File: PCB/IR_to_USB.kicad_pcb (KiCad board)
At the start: 2 copper layers, 120.7 x 44.4 mm, 5 parts, among them U1 STM32F070CBT6

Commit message: PCB in progress
Signed-off-by: denis-m-tyurin <denis.m.turin@gmail.com>
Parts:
- added C5: 100 nF, Capacitors_SMD:C_1206_HandSoldering, F.Cu at (145.2, 94.4)
- added C6: 100 nF, Capacitors_SMD:C_1206_HandSoldering, F.Cu at (136.6, 76.3)
- added C7: 100 nF, Capacitors_SMD:C_1206_HandSoldering, F.Cu at (130.6, 88.5)
- added C8: 100 nF, Capacitors_SMD:C_1206_HandSoldering, F.Cu at (130.4, 79.2)
- added D1: LED_RGB, LEDs:LED_RGB_PLLC-6, F.Cu at (122.1, 95.3)
- added JP1: JUMPER, Buttons_Switches_ThroughHole:SW_DIP_x1_Slide, F.Cu at (138.7, 72.7)
- added P1: CONN_01X06, Connect:PINHEAD1-6, F.Cu at (153.0, 70.9)
- added P2: USB_OTG, Connect:USB_Mini-B, F.Cu at (171.1, 100.8)
- added R1: 10K, Resistors_SMD:R_1206_HandSoldering, F.Cu at (142.4, 74.2)
- added R2: 10K, Resistors_SMD:R_1206_HandSoldering, F.Cu at (128.4, 74.2)
- added R3: 62, Resistors_SMD:R_1206_HandSoldering, F.Cu at (130.1, 94.3)
- added R4: 5, Resistors_SMD:R_1206_HandSoldering, F.Cu at (130.1, 97.3)
- added R5: 5, Resistors_SMD:R_1206_HandSoldering, F.Cu at (130.2, 100.6)
- added R6: 33, Resistors_SMD:R_1206_HandSoldering, F.Cu at (156.9, 94.5)
- added R7: 33, Resistors_SMD:R_1206_HandSoldering, F.Cu at (163.6, 90.2)
- added SW1: SW_PUSH, Buttons_Switches_ThroughHole:SW_PUSH-12mm, F.Cu at (121.2, 84.7)
- added U2: STM32F070CBT6, Housings_QFP:LQFP-48_7x7mm_Pitch0.5mm, F.Cu at (140.9, 85.8)
- added U3: TSOP48, TO_SOT_Packages_THT:TO-220_Neutral123_Horizontal_LargePads, F.Cu at (140.2, 100.3)
- added X1: CRYSTAL_SMD, Footprint_lib:CSTCE_G_Murata_Resonator, F.Cu at (131.1, 81.7)
- C1, C2, C4: footprint Capacitors_SMD:C_1206 -> Capacitors_SMD:C_1206_HandSoldering
- C3: value 100 nF -> 330 nF; footprint Capacitors_SMD:C_1206 -> Capacitors_SMD:C_1206_HandSoldering
- U1: value STM32F070CBT6 -> L78L; footprint Housings_QFP:LQFP-48_7x7mm_Pitch0.5mm -> TO_SOT_Packages_THT:TO-92_Inline_Narrow_Oval
- moved C3 77.1 mm to (168.4, 118.4), turned to 0 degrees
- moved U1 58.7 mm to (158.8, 114.7)
- moved C1 55.5 mm to (159.4, 122.7)
- moved C2 47.8 mm to (150.6, 82.9)
- moved C4 9.70 mm to (124.5, 81.3), turned to 270 degrees
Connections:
- C1 pad 1: Earth -> +3V3
- C1 pad 2: +3V3 -> Earth
- C3 pad 1: Earth -> +5V
- C3 pad 2: +3V3 -> Earth
- C4 pad 2: +3V3 -> Net-(C4-Pad2)
- U1 pad 1: Net-(U1-Pad1) -> +3V3
- U1 pad 2: Net-(U1-Pad2) -> Earth
- U1 pad 3: Net-(U1-Pad3) -> +5V
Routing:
- net Earth: track 38.3 -> 155.6 mm
- net Net-(C4-Pad2): track 0.00 -> 73.8 mm
- net Net-(P1-Pad3): track 0.00 -> 28.3 mm
- net Net-(P1-Pad4): track 0.00 -> 17.1 mm
- net Net-(R5-Pad1): track 0.00 -> 14.7 mm
- net +3V3: track 85.8 -> 98.4 mm
- net Net-(R4-Pad1): track 0.00 -> 11.9 mm
- net Net-(JP1-Pad2): track 0.00 -> 11.6 mm
- net Net-(U2-Pad16): track 0.00 -> 11.4 mm
- net Net-(R3-Pad1): track 0.00 -> 9.26 mm
- net Net-(U2-Pad6): track 0.00 -> 7.51 mm
- net Net-(D1-Pad4): track 0.00 -> 7.34 mm
- net Net-(D1-Pad5): track 0.00 -> 5.28 mm
- net Net-(U2-Pad5): track 0.00 -> 4.73 mm
- net Net-(D1-Pad6): track 0.00 -> 4.49 mm
- removed copper zone on F.Cu, net Earth
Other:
- board size 120.7 x 44.4 mm -> 140.5 x 67.6 mm

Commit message: First PCB draft
Signed-off-by: denis-m-tyurin <denis.m.turin@gmail.com>
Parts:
- added  : R0, Resistors_SMD:R_1206_HandSoldering, F.Cu at (137.4, 107.7)
- added  : R0, Resistors_SMD:R_1206_HandSoldering, F.Cu at (135.0, 68.5)
- added  : R0, Resistors_SMD:R_1206_HandSoldering, F.Cu at (158.1, 74.7)
- added  : R0, Resistors_SMD:R_1206_HandSoldering, F.Cu at (139.3, 98.4)
- added  : R0, Resistors_SMD:R_1206_HandSoldering, F.Cu at (144.8, 97.5)
- moved C1 26.9 mm to (153.8, 96.4), turned to 270 degrees
- moved C3 24.5 mm to (148.3, 104.4), turned to 180 degrees
- moved U1 18.1 mm to (150.3, 98.7), turned to 270 degrees
- moved R7 11.7 mm to (152.0, 89.1), turned to 180 degrees
- moved P2 9.93 mm to (161.2, 100.0), turned to 180 degrees
- moved U3 4.11 mm to (139.9, 104.4)
- moved R6 3.78 mm to (159.2, 91.5), turned to 180 degrees
- moved C8 0.90 mm to (130.4, 78.3)
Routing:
- net +3V3: track 98.4 -> 234.7 mm
- net Earth: track 155.6 -> 201.9 mm
- net Net-(P2-Pad2): track 0.00 -> 20.1 mm
- net Net-(P2-Pad3): track 0.00 -> 20.0 mm
- net Net-(R6-Pad2): track 0.00 -> 17.3 mm
- net +5V: track 0.00 -> 10.8 mm
- net Net-(R7-Pad2): track 0.00 -> 7.92 mm
- net Net-(P1-Pad3): track 28.3 -> 33.9 mm
- net Net-(U2-Pad16): track 11.4 -> 13.2 mm
- net Net-(C4-Pad2): track 73.8 -> 72.6 mm
- added copper zone on F.Cu, net Earth
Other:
- board size 140.5 x 67.6 mm -> 63 x 71 mm
- rule trace_min: 0.01 -> 0.2

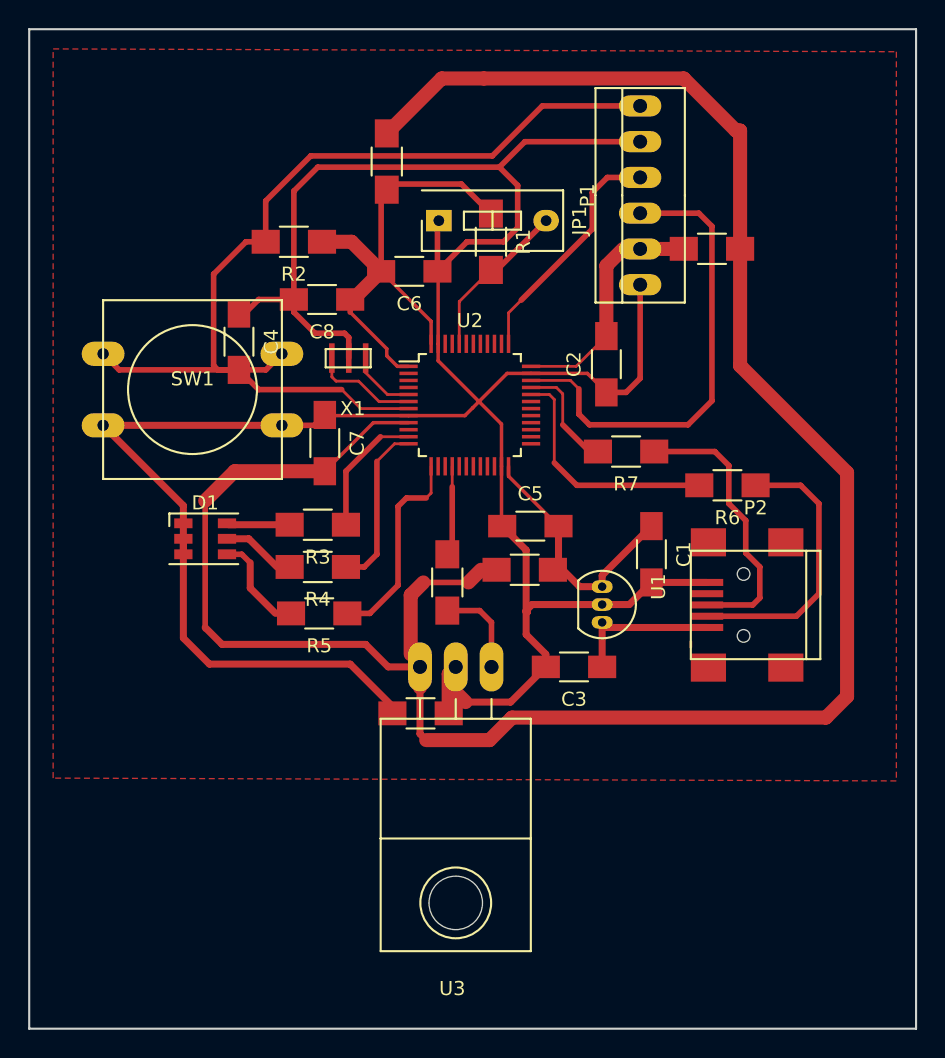
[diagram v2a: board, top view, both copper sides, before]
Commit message: Rework PCB: changed RGB led type, removed reset button, etc.
Signed-off-by: denis-m-tyurin <denis.m.turin@gmail.com>
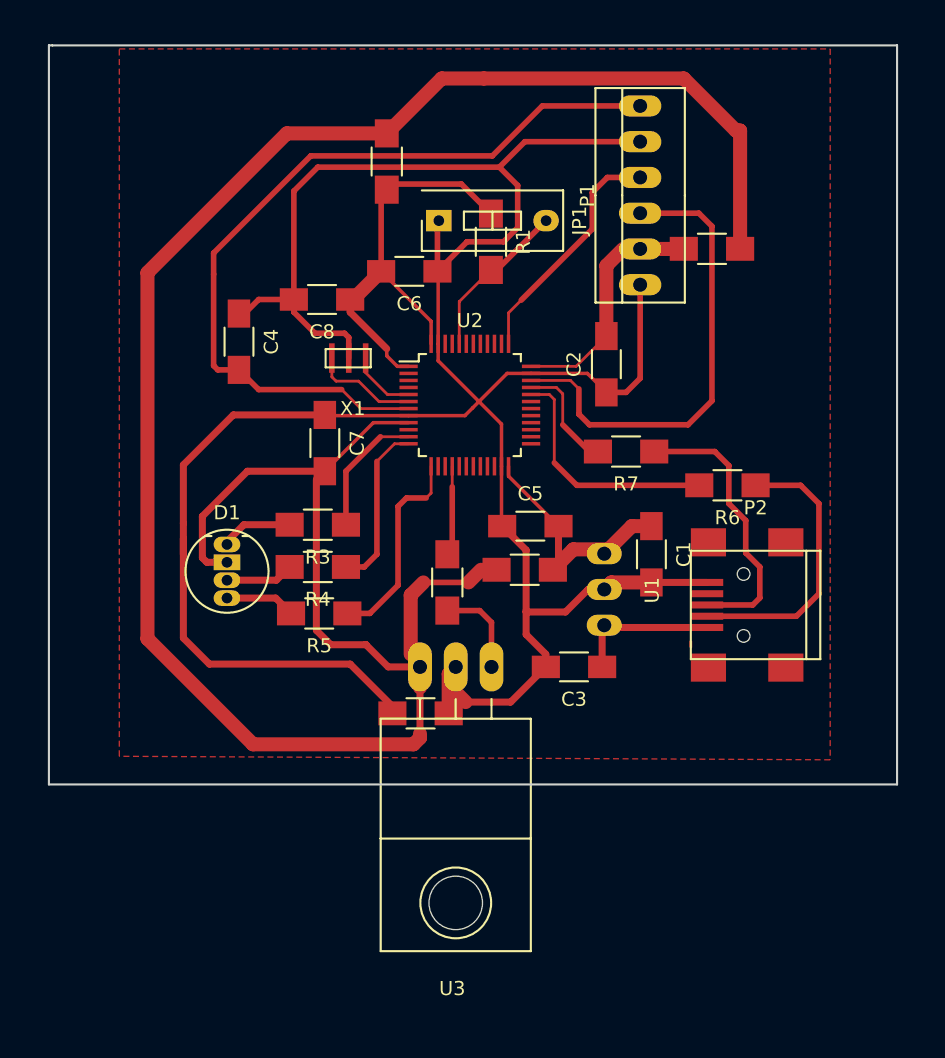
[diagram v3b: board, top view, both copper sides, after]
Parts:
- removed R2: 10K, Resistors_SMD:R_1206_HandSoldering
- removed SW1: SW_PUSH, Buttons_Switches_ThroughHole:SW_PUSH-12mm
- D1: value LED_RGB -> LED_RABG; footprint LEDs:LED_RGB_PLLC-6 -> LEDs:LED-RGB-5MM_Common_Cathode
- U1: footprint TO_SOT_Packages_THT:TO-92_Inline_Narrow_Oval -> TO_SOT_Packages_THT:TO-220_Neutral123_PadsOnly
- moved D1 1.60 mm to (123.7, 95.7)
- moved U1 0.25 mm to (150.4, 98.9)
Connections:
- D1 pad 1: Earth -> Net-(D1-Pad1)
- D1 pad 2: Earth -> +3V3
- D1 pad 3: Earth -> Net-(D1-Pad3)
- R3 pad 2: Net-(D1-Pad6) -> Net-(D1-Pad1)
- R4 pad 2: Net-(D1-Pad5) -> Net-(D1-Pad3)
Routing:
- net Net-(C4-Pad2): track 72.6 -> 58.1 mm
- net Earth: track 201.9 -> 192.1 mm
- net Net-(D1-Pad5): track 5.28 -> 0.00 mm
- net Net-(D1-Pad1): track 0.00 -> 5.15 mm
- net Net-(D1-Pad3): track 0.00 -> 4.84 mm
- net Net-(D1-Pad6): track 4.49 -> 0.00 mm
- net +3V3: track 234.7 -> 231.7 mm
- net Net-(D1-Pad4): track 7.34 -> 5.00 mm
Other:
- board size 63 x 71 mm -> 60.2 x 52.5 mm

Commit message: PCB ready
Signed-off-by: denis-m-tyurin <denis.m.turin@gmail.com>
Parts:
- moved P1 7.26 mm to (154.5, 78.0)
- moved   7.14 mm to (159.2, 81.8)
- moved D1 5.00 mm to (122.2, 100.5), turned to 90 degrees
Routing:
- net +3V3: track 231.7 -> 241.6 mm
- net Net-(P1-Pad3): track 33.9 -> 27.0 mm
- net Net-(P2-Pad2): track 20.1 -> 13.3 mm
- net Net-(D1-Pad1): track 5.15 -> 9.88 mm
- net Net-(P1-Pad4): track 17.1 -> 14.2 mm
- net Net-(D1-Pad4): track 5.00 -> 2.39 mm
- net Earth: track 192.1 -> 190.7 mm
- net Net-(C4-Pad2): track 58.1 -> 59.2 mm
- net Net-(P2-Pad3): track 20.0 -> 19.2 mm
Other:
- rule pad_to_mask_clearance: 0.2 -> 0.07

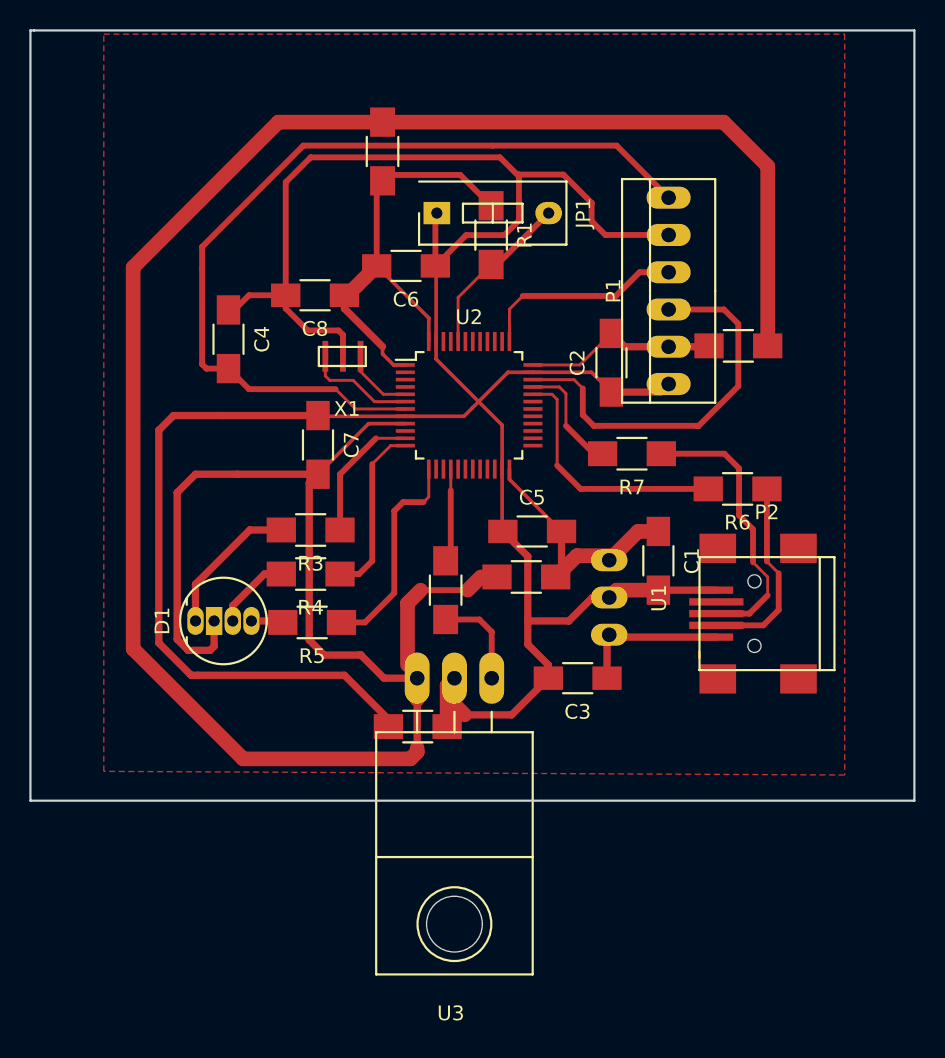
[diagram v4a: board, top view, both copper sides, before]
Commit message: Reworked PCB to double layers
Signed-off-by: denis-m-tyurin <denis.m.turin@gmail.com>
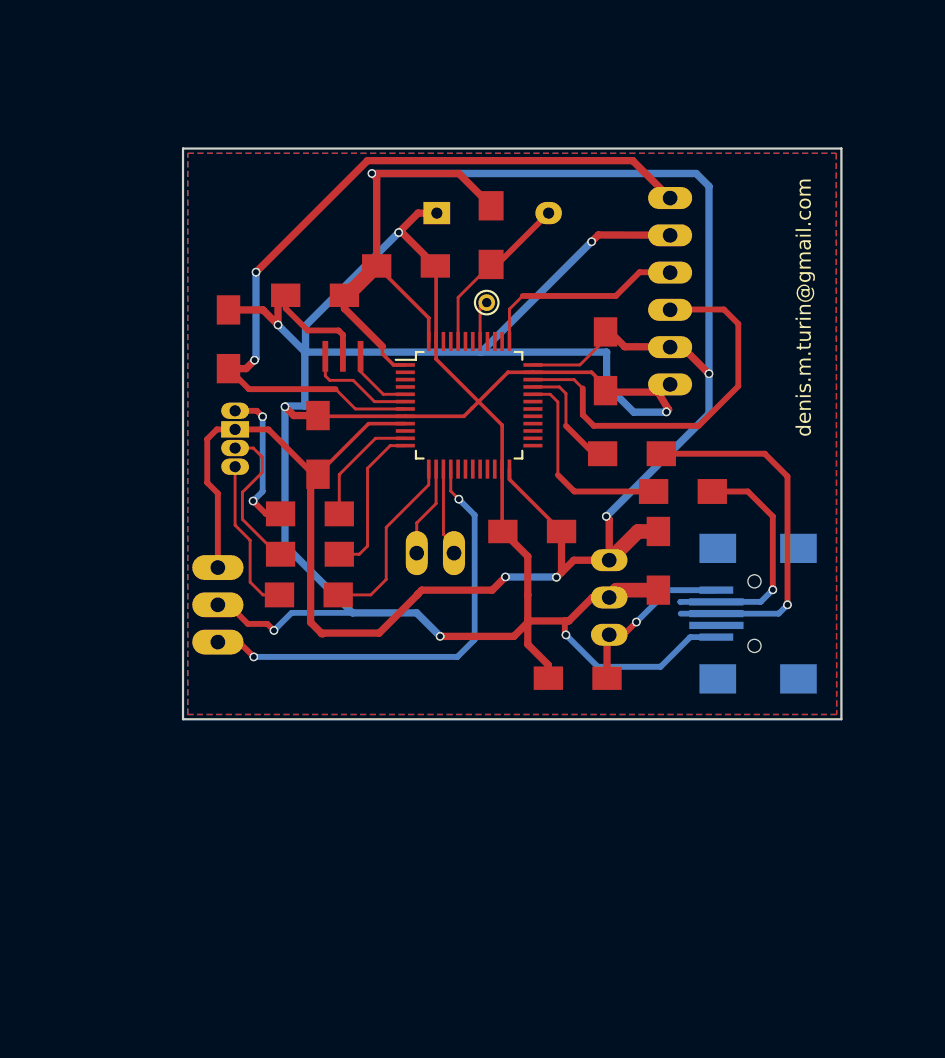
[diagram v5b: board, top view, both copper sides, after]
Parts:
- removed  : R0, Resistors_SMD:R_1206_HandSoldering (x5)
- added P3: CONN_01X02, Footprint_lib:PINHEAD1-2_withoutSilk, F.Cu at (138.6, 95.9)
- added P4: CONN_01X01, Connect:PINTST, F.Cu at (142.1, 78.8)
- C1, C2, C3, C4, C5, C6, C7, C8: footprint Capacitors_SMD:C_1206_HandSoldering -> Footprint_lib:C_1206_HandSoldering_withoutSilk
- D1: footprint LEDs:LED-RGB-5MM_Common_Cathode -> Footprint_lib:LED-RGB-5MM_Common_Cathode_DENIS
- JP1: footprint Buttons_Switches_ThroughHole:SW_DIP_x1_Slide -> Footprint_lib:SW_DIP_x1_Slide_DENIS
- P1: footprint Connect:PINHEAD1-6 -> Footprint_lib:PINHEAD1-6_DENIS
- P2: moved to B.Cu
- R1, R3, R4, R5, R6, R7: footprint Resistors_SMD:R_1206_HandSoldering -> Footprint_lib:R_1206_HandSoldering_withoutSilk
- U3: footprint TO_SOT_Packages_THT:TO-220_Neutral123_Horizontal_LargePads -> Footprint_lib:TO-220_Neutral123_Horizontal_LargePads_withoutSilk
- X1: footprint Footprint_lib:CSTCE_G_Murata_Resonator -> Footprint_lib:CSTCE_G_Murata_Resonator_withoutSilk
- moved U3 16.9 mm to (123.8, 99.4), turned to 90 degrees
- moved D1 14.6 mm to (125.0, 86.2), turned to 0 degrees
- moved R6 3.73 mm to (155.5, 91.7)
- moved R5 1.89 mm to (130.0, 98.7)
- moved R4 1.35 mm to (130.1, 96.0)
- moved R3 1.10 mm to (130.1, 93.2)
- moved C2 0.41 mm to (150.2, 82.8)
- moved P1 0.10 mm to (154.6, 78.0)
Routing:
- net +3V3: track 241.6 -> 168.8 mm, vias 0 -> 5
- net Net-(U2-Pad16): track 13.2 -> 30.7 mm, vias 0 -> 2
- net Earth: track 190.7 -> 203.6 mm, vias 0 -> 8
- net Net-(D1-Pad4): track 2.39 -> 10.7 mm
- net Net-(P2-Pad3): track 19.2 -> 25.5 mm, vias 0 -> 1
- net Net-(P3-Pad1): track 0.00 -> 6.27 mm
- net Net-(P3-Pad2): track 0.00 -> 6.02 mm
- net Net-(C4-Pad2): track 59.2 -> 53.6 mm, vias 0 -> 2
- net Net-(D1-Pad3): track 5.24 -> 10.5 mm
- net Net-(R6-Pad2): track 17.3 -> 13.9 mm
- net Net-(P2-Pad2): track 13.3 -> 16.5 mm, vias 0 -> 1
- net Net-(P4-Pad1): track 0.00 -> 3.05 mm
- net Net-(R5-Pad1): track 14.7 -> 12.4 mm
- net +5V: track 10.8 -> 12.2 mm, vias 0 -> 1
- net Net-(R4-Pad1): track 11.9 -> 10.7 mm
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- added copper zone on B.Cu, net Earth
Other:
- board size 60.2 x 52.5 mm -> 44.9 x 38.9 mm
- board text added: "+3v"
- board text added: "DEBUG"
- board text added: "GND"
- board text added: "RST"
- board text added: "SWC"
- board text added: "SWD"
- board text added: "TDM"
- board text added: "USB"
- board text added: "boot mode"
- board text added: "denis.m.turin@gmail.com"
